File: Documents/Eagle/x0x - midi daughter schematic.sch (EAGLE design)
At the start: 29 parts

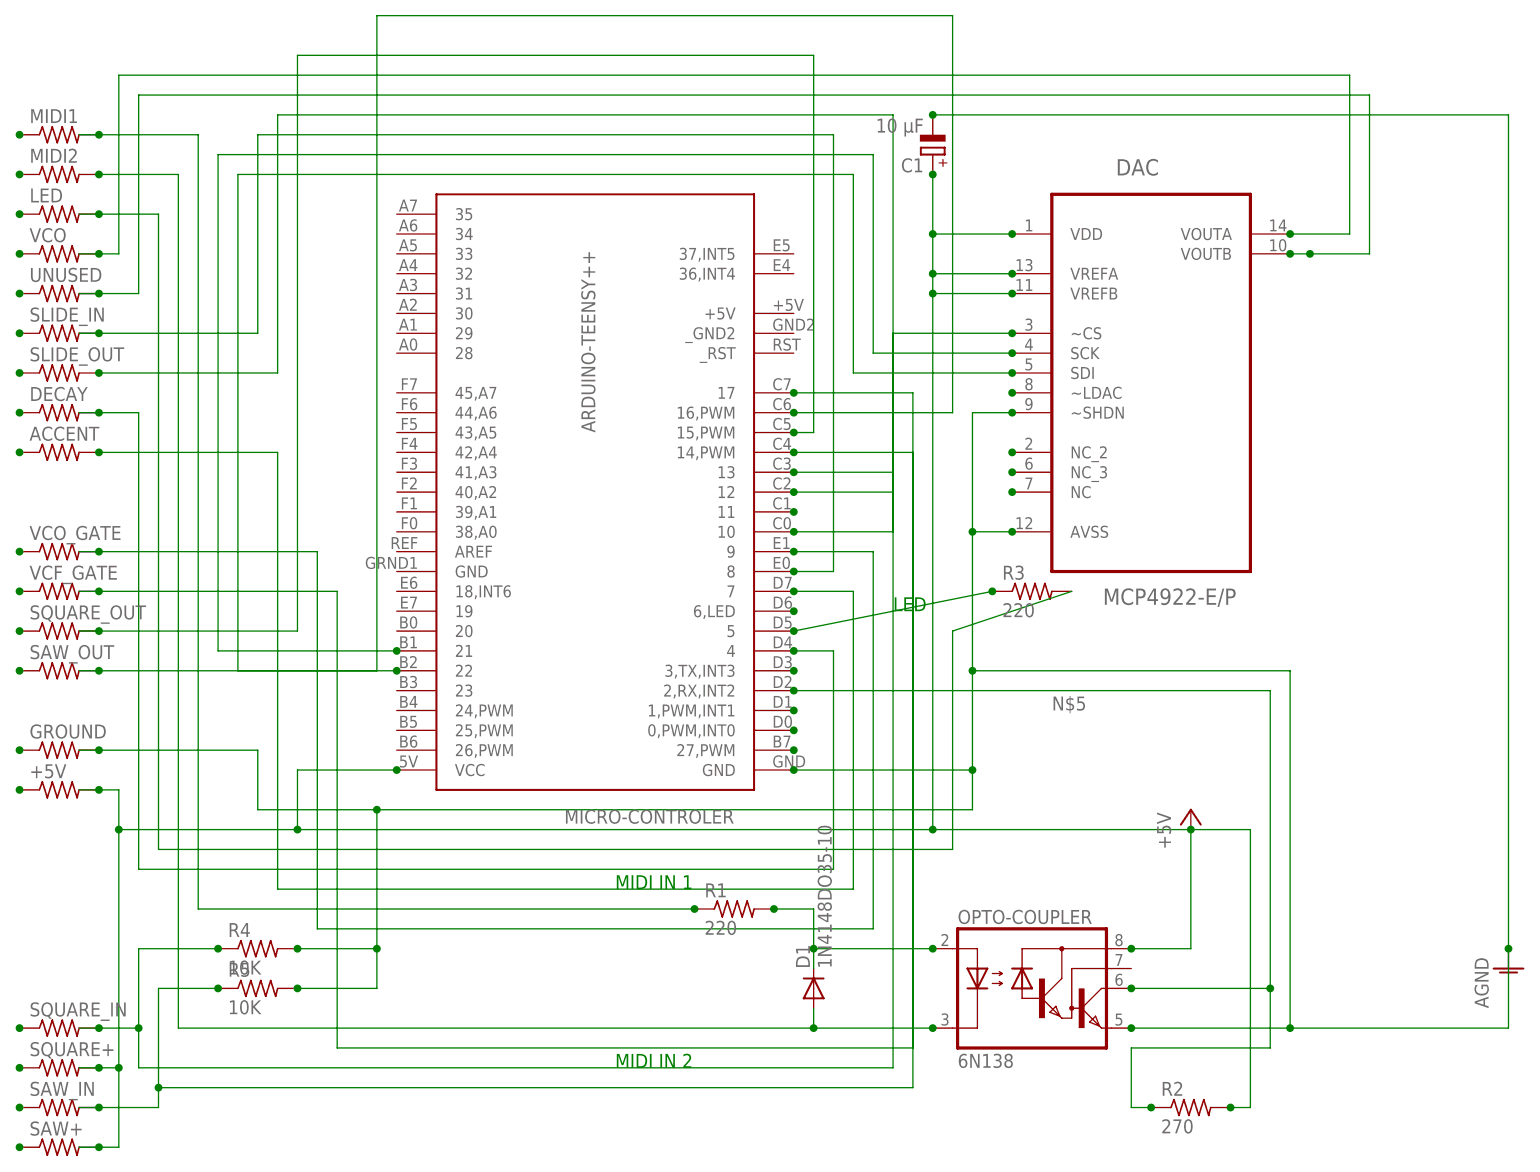
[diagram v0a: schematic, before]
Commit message: Fix DAC shutdown/latch wiring, revise firmware, document changes
Schematic (.sch) — netlist corrections (verified by re-parse, ERC/DRC
still required in Eagle):
- MCP4922 ~SHDN (pin 9) moved from AGND to +5V. It was tied to ground,
  which holds both DAC outputs in permanent hardware shutdown.
- ~LDAC (pin 8) now wired to MCU pin 11; both were floating stubs, so
  the DAC latch line was never connected.
- VOUTB connector pad renamed UNUSED -> VCF_CUTOFF (.sch + .brd) to
  document the VCF cutoff output intent.

NOTE: board copper was intentionally NOT hand-edited — moving the ~SHDN
net while leaving old traces would short +5V to GND. The .brd is left
for Eagle to reconcile (ERC -> forward-annotate -> re-route ~SHDN and
~LDAC airwires -> DRC).

Firmware (.ino):
- WriteDAC(channel, value) builds the 16-bit word per channel, enabling
  channel B (VCF); VCF cutoff driven from MIDI CC 74.
- Non-blocking LED blink (millis) removes 25 ms gate latency on Note On.
- Monophonic note stack (last-note priority) prevents Note Off of an
  inactive note from cutting the gate.
- MIDI input filtered to MIDIChannel instead of OMNI.
- Removed dead code (shadowed `type`, unused Uart, stray PIN_D2/PIN_D3).

README updated to match.

Co-Authored-By: Claude Opus 4.8 <noreply@anthropic.com>
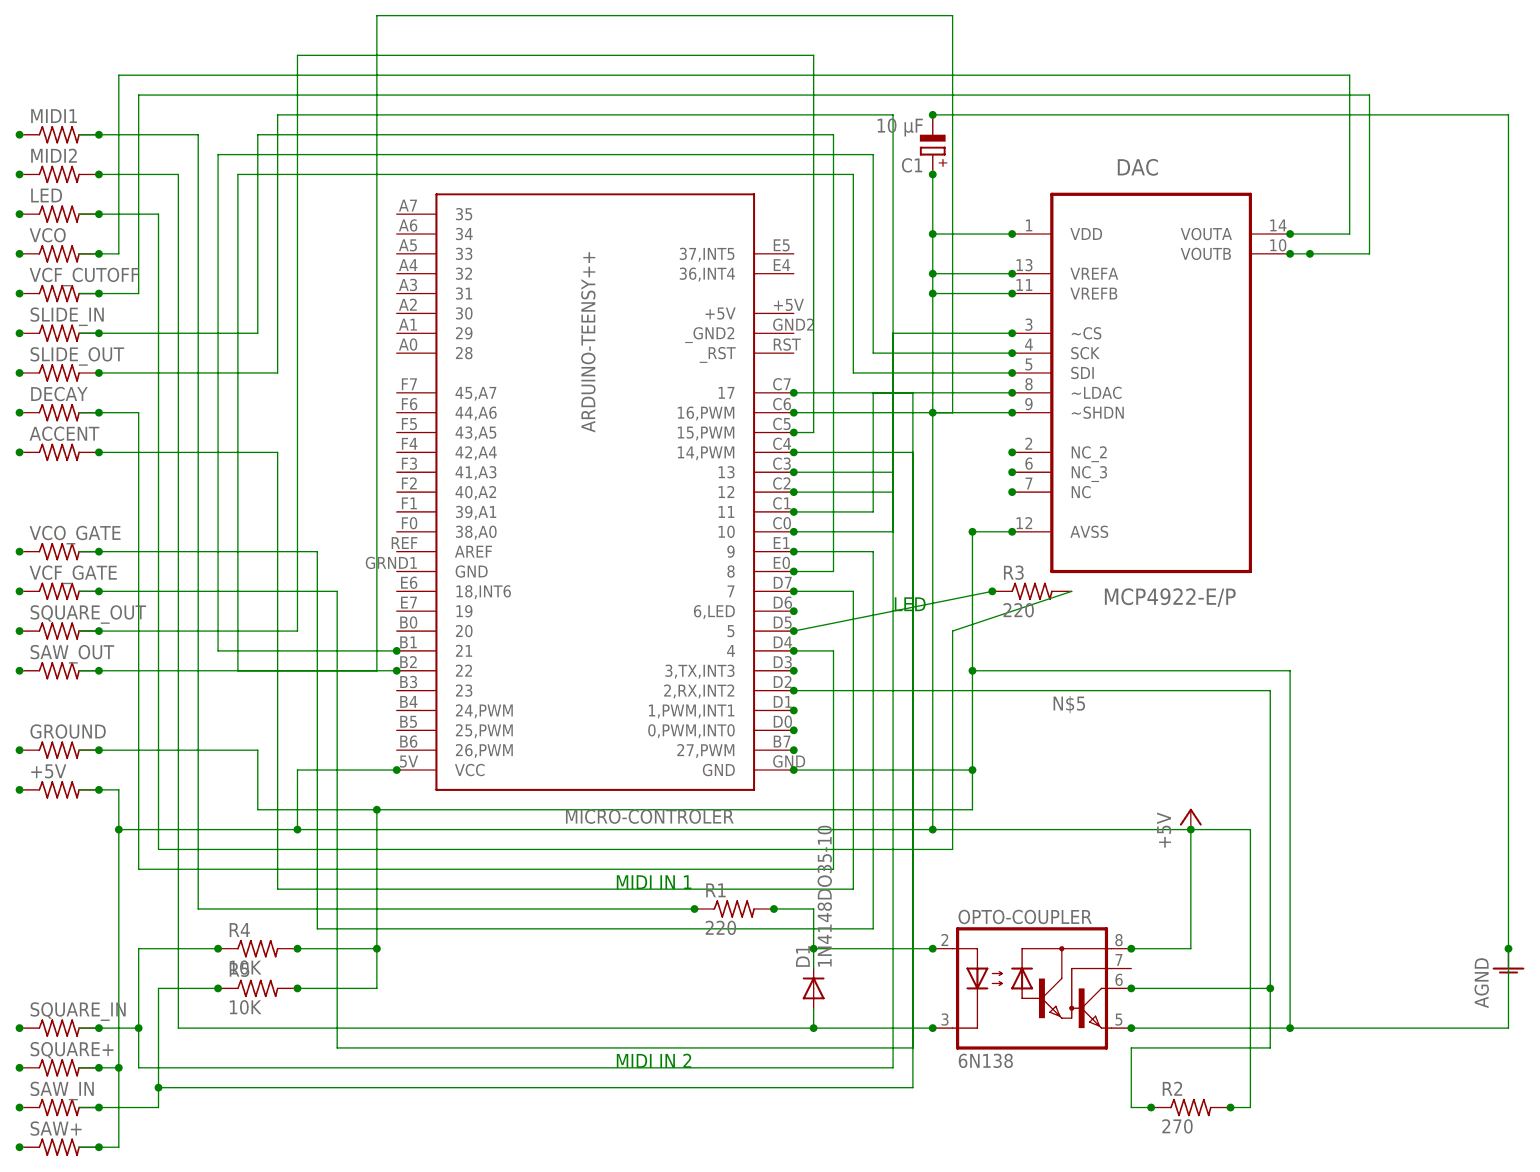
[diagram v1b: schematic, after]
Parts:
- renumbered UNUSED to VCF_CUTOFF
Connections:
- removed net N$45: MICRO-CONTROLER.11
- net +5V: now also DAC.~SHDN
- net AGND: no longer DAC.~SHDN
- net N$41: now also MICRO-CONTROLER.11
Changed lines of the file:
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@@
 <part name="LED" library="rcl" deviceset="R-US_" device="0207/10"/>
 <part name="VCO" library="rcl" deviceset="R-US_" device="0207/10"/>
-<part name="UNUSED" library="rcl" deviceset="R-US_" device="0207/10"/>
+<part name="VCF_CUTOFF" library="rcl" deviceset="R-US_" device="0207/10"/>
 <part name="SLIDE_IN" library="rcl" deviceset="R-US_" device="0207/10"/>
 <part name="SLIDE_OUT" library="rcl" deviceset="R-US_" device="0207/10"/>
@@
 <instance part="LED" gate="G$1" x="-101.6" y="137.16"/>
 <instance part="VCO" gate="G$1" x="-101.6" y="132.08"/>
-<instance part="UNUSED" gate="G$1" x="-101.6" y="127"/>
+<instance part="VCF_CUTOFF" gate="G$1" x="-101.6" y="127"/>
 <instance part="SLIDE_IN" gate="G$1" x="-101.6" y="121.92"/>
 <instance part="SLIDE_OUT" gate="G$1" x="-101.6" y="116.84"/>
@@
 <wire x1="10.16" y1="149.86" x2="83.82" y2="149.86" width="0.1524" layer="91"/>
 <wire x1="83.82" y1="149.86" x2="83.82" y2="43.18" width="0.1524" layer="91"/>
-<pinref part="DAC" gate="A" pin="~SHDN"/>
-<wire x1="20.32" y1="111.76" x2="15.24" y2="111.76" width="0.1524" layer="91"/>
-<wire x1="15.24" y1="111.76" x2="15.24" y2="96.52" width="0.1524" layer="91"/>
 <pinref part="DAC" gate="A" pin="AVSS"/>
 <wire x1="15.24" y1="96.52" x2="20.32" y2="96.52" width="0.1524" layer="91"/>
@@
 <junction x="-71.12" y="38.1"/>
 <junction x="10.16" y="149.86"/>
-<junction x="20.32" y="111.76"/>
 <junction x="20.32" y="96.52"/>
 <junction x="-7.62" y="66.04"/>
@@
 <junction x="10.16" y="129.54"/>
 <wire x1="10.16" y1="129.54" x2="10.16" y2="127" width="0.1524" layer="91"/>
-<wire x1="10.16" y1="127" x2="10.16" y2="58.42" width="0.1524" layer="91"/>
+<wire x1="10.16" y1="127" x2="10.16" y2="111.76" width="0.1524" layer="91"/>
+<wire x1="10.16" y1="111.76" x2="10.16" y2="58.42" width="0.1524" layer="91"/>
+<junction x="10.16" y="111.76"/>
+<pinref part="DAC" gate="A" pin="~SHDN"/>
+<wire x1="10.16" y1="111.76" x2="20.32" y2="111.76" width="0.1524" layer="91"/>
+<junction x="20.32" y="111.76"/>
 <wire x1="10.16" y1="58.42" x2="43.18" y2="58.42" width="0.1524" layer="91"/>
 <wire x1="-71.12" y1="58.42" x2="10.16" y2="58.42" width="0.1524" layer="91"/>
@@
 <wire x1="-91.44" y1="152.4" x2="-91.44" y2="127" width="0.1524" layer="91"/>
 <wire x1="-91.44" y1="127" x2="-96.52" y2="127" width="0.1524" layer="91"/>
-<pinref part="UNUSED" gate="G$1" pin="2"/>
+<pinref part="VCF_CUTOFF" gate="G$1" pin="2"/>
 <wire x1="-96.52" y1="127" x2="-99.06" y2="127" width="0.1524" layer="91"/>
 <junction x="-96.52" y="127"/>
@@
 <net name="N$36" class="0">
 <segment>
-<pinref part="UNUSED" gate="G$1" pin="1"/>
+<pinref part="VCF_CUTOFF" gate="G$1" pin="1"/>
 <junction x="-106.68" y="127"/>
 </segment>
@@
 <segment>
 <pinref part="DAC" gate="A" pin="~LDAC"/>
+<pinref part="MICRO-CONTROLER" gate="G$1" pin="11"/>
+<wire x1="-7.62" y1="99.06" x2="2.54" y2="99.06" width="0.1524" layer="91"/>
+<wire x1="2.54" y1="99.06" x2="2.54" y2="114.3" width="0.1524" layer="91"/>
+<wire x1="2.54" y1="114.3" x2="20.32" y2="114.3" width="0.1524" layer="91"/>
 <junction x="20.32" y="114.3"/>
+<junction x="-7.62" y="99.06"/>
 </segment>
 </net>
@@
 </segment>
 </net>
-<net name="N$45" class="0">
-<segment>
-<pinref part="MICRO-CONTROLER" gate="G$1" pin="11"/>
-<junction x="-7.62" y="99.06"/>
-</segment>
-</net>
